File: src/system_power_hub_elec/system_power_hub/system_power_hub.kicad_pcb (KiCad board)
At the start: 6 copper layers, 65 x 65 mm, 127 parts, among them J1 XT90M, J101 SM02B-PASS, J2 XT60F, J3 SM02B-PASS, J4 XT60F, J6 IDC6, J8 XT60F, J9 XT60F, Q1 SSM3K333R, Q10 IRFH7440TRPBF, Q2 Q_Dual_NPN_NPN_E1B1C2E2B2C1, Q3 IRFH7440TRPBF, Q4 IRFH7440TRPBF, Q8 Q_Dual_NPN_NPN_E1B1C2E2B2C1, Q9 IRFH7440TRPBF, U102 TCAN1462V, U2 STM32G474RBT6, U220 MP2459GJ-Z-MS, U230 AP62200TWU, U4 24LC128, Y1 24MHz

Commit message: Draft SPM PCB layout
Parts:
- removed U2: STM32G474RBT6, Package_QFP:LQFP-64_10x10mm_P0.5mm
- added C32: 100n, Capacitor_SMD:C_0603_1608Metric, B.Cu at (141.4, 57.8)
- added C33: 1u, Capacitor_SMD:C_1206_3216Metric, B.Cu at (146.3, 60.5)
- added C34: 100n, Capacitor_SMD:C_0603_1608Metric, B.Cu at (78.1, 128.5)
- added C35: 100n, Capacitor_SMD:C_0603_1608Metric, B.Cu at (73.1, 128.5)
- added C38: 1n, Capacitor_SMD:C_0402_1005Metric, B.Cu at (83.8, 114.4)
- added C39: 1n, Capacitor_SMD:C_0402_1005Metric, B.Cu at (84.1, 124.9)
- added C40: 1n, Capacitor_SMD:C_0402_1005Metric, B.Cu at (66.6, 114.4)
- added C41: 1n, Capacitor_SMD:C_0402_1005Metric, B.Cu at (65.9, 125.0)
- added C42: 100n, Capacitor_SMD:C_0603_1608Metric, B.Cu at (112.4, 128.4)
- added C43: 100n, Capacitor_SMD:C_0603_1608Metric, B.Cu at (107.4, 128.5)
- added C44: 1n, Capacitor_SMD:C_0402_1005Metric, B.Cu at (118.1, 114.3)
- added C45: 1n, Capacitor_SMD:C_0402_1005Metric, B.Cu at (118.3, 124.8)
- added C46: 1n, Capacitor_SMD:C_0402_1005Metric, B.Cu at (100.9, 114.3)
- added C47: 1n, Capacitor_SMD:C_0402_1005Metric, B.Cu at (100.2, 124.9)
- added C48: 1n, Capacitor_SMD:C_0402_1005Metric, B.Cu at (118.3, 128.9)
- added C49: 1n, Capacitor_SMD:C_0402_1005Metric, B.Cu at (100.2, 128.6)
- added C50: 1n, Capacitor_SMD:C_0402_1005Metric, B.Cu at (84.0, 128.9)
- added C51: 1n, Capacitor_SMD:C_0402_1005Metric, B.Cu at (65.9, 128.6)
- added D4: SBR0560S1-7, Diode_SMD:D_SOD-123, B.Cu at (146.2, 53.8)
- added D5: SBR0560S1-7, Diode_SMD:D_SOD-123, B.Cu at (146.2, 57.1)
- added J5: XT30F, Connector_AMASS:AMASS_XT30PW-F_1x02_P2.50mm_Horizontal, F.Cu at (69.3, 117.3)
- added J7: XT30F, Connector_AMASS:AMASS_XT30PW-F_1x02_P2.50mm_Horizontal, F.Cu at (120.8, 117.3)
- added J8: XT30F, Connector_AMASS:AMASS_XT30PW-F_1x02_P2.50mm_Horizontal, F.Cu at (103.6, 117.3)
- added Q10: IRFH7440TRPBF, Bluesat:PQFN_5x6mm_E_SGD, B.Cu at (103.6, 127.6)
- added Q11: IRFH7440TRPBF, Bluesat:PQFN_5x6mm_E_SGD, B.Cu at (69.4, 127.6)
- added Q5: SSM3K333R, Package_TO_SOT_SMD:SOT-23-3, B.Cu at (140.8, 54.3)
- added Q6: Q_Dual_NPN_NPN_E1B1C2E2B2C1, Package_TO_SOT_SMD:SOT-363_SC-70-6, B.Cu at (75.6, 126.9)
- added Q7: IRFH7440TRPBF, Bluesat:PQFN_5x6mm_E_SGD, B.Cu at (87.5, 127.8)
- added Q8: Q_Dual_NPN_NPN_E1B1C2E2B2C1, Package_TO_SOT_SMD:SOT-363_SC-70-6, B.Cu at (109.9, 126.8)
- added Q9: IRFH7440TRPBF, Bluesat:PQFN_5x6mm_E_SGD, B.Cu at (121.7, 127.7)
- added R16: 10k, Resistor_SMD:R_0402_1005Metric, B.Cu at (109.9, 130.0)
- added R18: 100R, Resistor_SMD:R_0402_1005Metric, B.Cu at (141.9, 60.1)
- added R20: 470k, Resistor_SMD:R_0402_1005Metric, B.Cu at (141.9, 62.1)
- added R21: 10k, Resistor_SMD:R_0402_1005Metric, B.Cu at (109.9, 123.6)
- added R22: 470k, Resistor_SMD:R_0402_1005Metric, B.Cu at (112.3, 125.3)
- added R23: 470k, Resistor_SMD:R_0402_1005Metric, B.Cu at (107.5, 125.3)
- added R24: 10k, Resistor_SMD:R_0402_1005Metric, B.Cu at (75.6, 130.1)
- added R25: 10k, Resistor_SMD:R_0402_1005Metric, B.Cu at (75.6, 123.7)
- added R26: 1m, Resistor_SMD:R_2512_6332Metric, B.Cu at (115.6, 127.3)
- added R27: 1m, Resistor_SMD:R_2512_6332Metric, B.Cu at (97.4, 127.5)
- added R28: 470k, Resistor_SMD:R_0402_1005Metric, B.Cu at (78.0, 125.4)
- added R29: 470k, Resistor_SMD:R_0402_1005Metric, B.Cu at (73.2, 125.4)
- added R30: 1m, Resistor_SMD:R_2512_6332Metric, B.Cu at (81.3, 127.4)
- added R31: 1m, Resistor_SMD:R_2512_6332Metric, B.Cu at (63.1, 127.6)
- added U1: STM32G474RBT6, Package_QFP:LQFP-64_10x10mm_P0.5mm, B.Cu at (146.0, 88.9)
- J1: value XT90M -> XT60M; footprint Connector_AMASS:AMASS_XT90PW-M_1x02_P10.90mm_Horizontal -> Connector_AMASS:AMASS_XT60IPW-M_1x03_P7.20mm_Horizontal
- J10: renamed from J9; value XT60F -> XT30F; footprint Connector_AMASS:AMASS_XT60PW-F_1x02_P7.20mm_Horizontal -> Connector_AMASS:AMASS_XT30PW-F_1x02_P2.50mm_Horizontal
- J2, J4: value XT60F -> XT30F; footprint Connector_AMASS:AMASS_XT60PW-F_1x02_P7.20mm_Horizontal -> Connector_AMASS:AMASS_XT30PW-F_1x02_P2.50mm_Horizontal
- J3: value SM02B-PASS -> XT30F; footprint Bluesat:SM02B-PASS -> Connector_AMASS:AMASS_XT30PW-F_1x02_P2.50mm_Horizontal
- J9: renamed from J8; value XT60F -> XT30F; footprint Connector_AMASS:AMASS_XT60PW-F_1x02_P7.20mm_Horizontal -> Connector_AMASS:AMASS_XT30PW-F_1x02_P2.50mm_Horizontal
- moved G*** 103.4 mm to (254.4, 108.5)
- moved C260 96.7 mm to (68.5, 108.8), turned to 180 degrees
- moved C261 91.7 mm to (68.8, 79.4), turned to 180 degrees
- moved J3 88.5 mm to (86.6, 117.3), turned to 180 degrees
- moved J101 78.9 mm to (209.2, 71.3), turned to -90 degrees
- moved R230 76.4 mm to (78.2, 77.4), turned to 0 degrees
- moved R231 75.0 mm to (78.2, 79.0), turned to 180 degrees
- moved R232 73.7 mm to (78.2, 80.6), turned to 180 degrees
- moved C231 72.5 mm to (82.4, 76.8), turned to 0 degrees
- moved C232 71.2 mm to (78.8, 82.8), turned to -90 degrees
- moved U230 69.9 mm to (82.4, 79.6), turned to 180 degrees
- moved C230 66.8 mm to (82.4, 83.2), turned to 0 degrees
- moved L230 66.5 mm to (87.2, 77.8), turned to 90 degrees
- moved D101 65.6 mm to (199.6, 71.3), turned to 180 degrees
- moved C12 64.6 mm to (70.0, 96.9)
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- renumbered C to C1, C to C250, C42 to C52, C43 to C53, C44 to C54, C45 to C55, C46 to C56, C47 to C57, C48 to C58, C49 to C59, Q4 to Q12, Q8 to Q13, Q9 to Q15, Q10 to Q16, Q3 to Q4, R16 to R32, R21 to R33, R22 to R34, R23 to R35, R26 to R36, R27 to R37, U to U240
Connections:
- C15 pad 1: GND -> Net-(U1A-PA2-opamp_vout_0)
- C16 pad 1: GND -> Net-(U1A-PA8-opamp_vout_1)
- C17 pad 1: GND -> Net-(U1A-PA6-opamp_vout_2)
- C18 pad 1: GND -> Net-(U1A-PB11-opamp_vout_3)
- D12 pad 1: Net-(D12-K) -> Vdrive
- J1 pad 1: VBUS -> GND
- J1 pad 2: GND -> VBUS
- J3 pad 1: Vdrive -> /Analog Stuff/vsense_p4
- J3 pad 2: Net-(D12-K) -> Net-(J3-Pin_2)
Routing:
- net /Analog Stuff/vsense_p3: track 87.1 -> 10.5 mm, vias 1 -> 0
- net Vdrive: track 138.0 -> 78.8 mm, vias 12 -> 9
- net /Analog Stuff/vsense_p0: track 68.7 -> 10.4 mm, vias 6 -> 0
- net /Analog Stuff/~{chan0}: track 57.8 -> 0.00 mm, vias 2 -> 1
- net /Analog Stuff/~{chan1}: track 54.5 -> 0.00 mm, vias 2 -> 1
- net /Analog Stuff/vsense_p1: track 54.7 -> 10.5 mm, vias 4 -> 0
- net /Analog Stuff/~{chan2}: track 39.1 -> 0.00 mm, vias 2 -> 1
- net /CANH: track 35.9 -> 0.11 mm
- net /CANL: track 35.4 -> 0.42 mm
- net /dbg.swdio: track 38.9 -> 6.46 mm, vias 2 -> 1
- net /dbg.swclk: track 36.5 -> 5.13 mm, vias 2 -> 1
- net /Analog Stuff/~{chan3}: track 28.4 -> 0.00 mm, vias 2 -> 1
- net /Analog Stuff/clk_in: track 27.5 -> 0.92 mm
- net Net-(U102-TXD): track 24.1 -> 0.07 mm
- net /dbg.swo: track 27.1 -> 3.26 mm, vias 3 -> 1
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- added copper zone on B.Cu, net /Analog Stuff/vsense_p4
- added copper zone on B.Cu, net /Analog Stuff/vsense_p5
- added copper zone on B.Cu, net /Analog Stuff/vsense_p6
- added copper zone on B.Cu, net /Analog Stuff/vsense_p7
- added copper zone on B.Cu, net Net-(J3-Pin_2)
- added copper zone on B.Cu, net Net-(J7-Pin_2)
- added copper zone on B.Cu, net Net-(J8-Pin_2)
- removed copper zone on B.Cu, net Net-(D12-K)
- removed copper zone on B.Cu, net Net-(J2-Pin_2)
- removed copper zone on In3.Cu, net VDD
- removed copper zone on B.Cu, net Vdrive
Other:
- board size 65 x 65 mm -> 66.5 x 77.6 mm
- board text added: "2nd charge pump (?)"
- board text added: "5V + RGB"
- board text added: "CAN"
- board text added: "EEPROM"
- board text added: "SWD"
- board text added: "WIP: Need to fix/swap pinout for xt30 connectors"
- board text added: "WIP: fix pin dir"
- board text added: "WIP: rearrange power circuits"
- board text added: "for opamps"

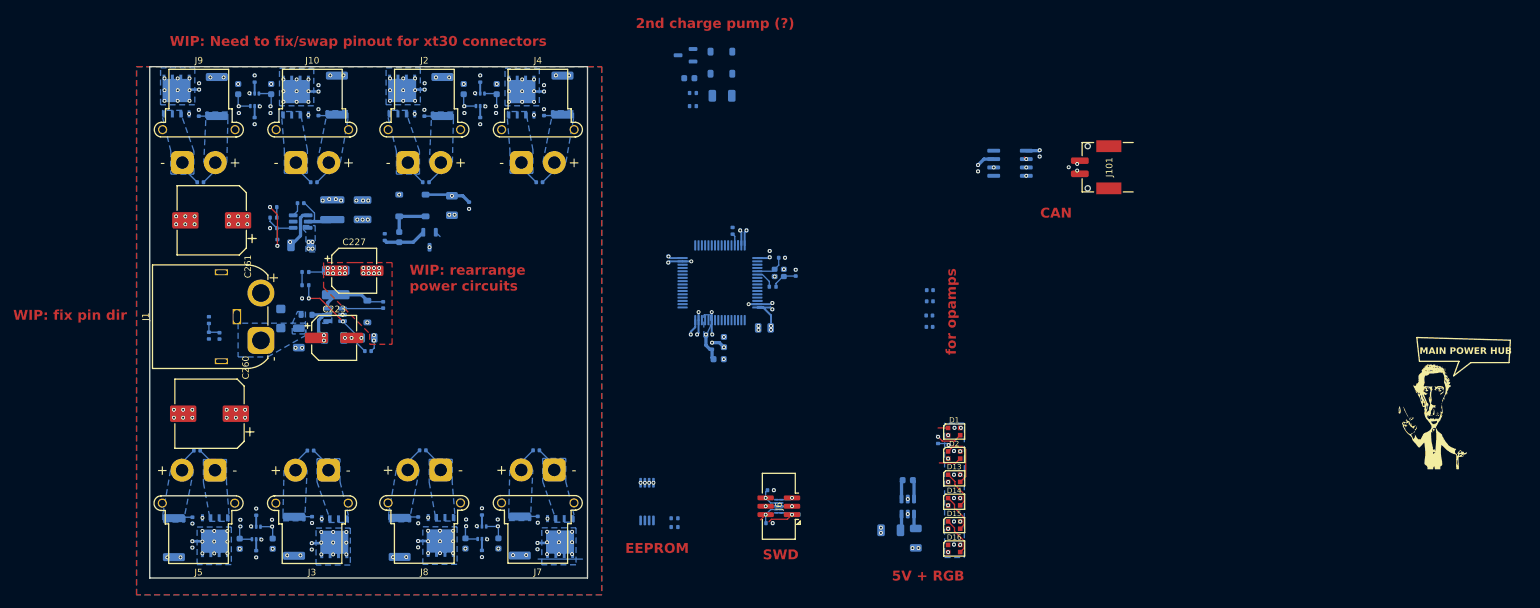
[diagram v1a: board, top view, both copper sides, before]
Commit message: Fixed XT connector routing, rewired power stuff (attempted to), made board smaller, more routing/layout progress
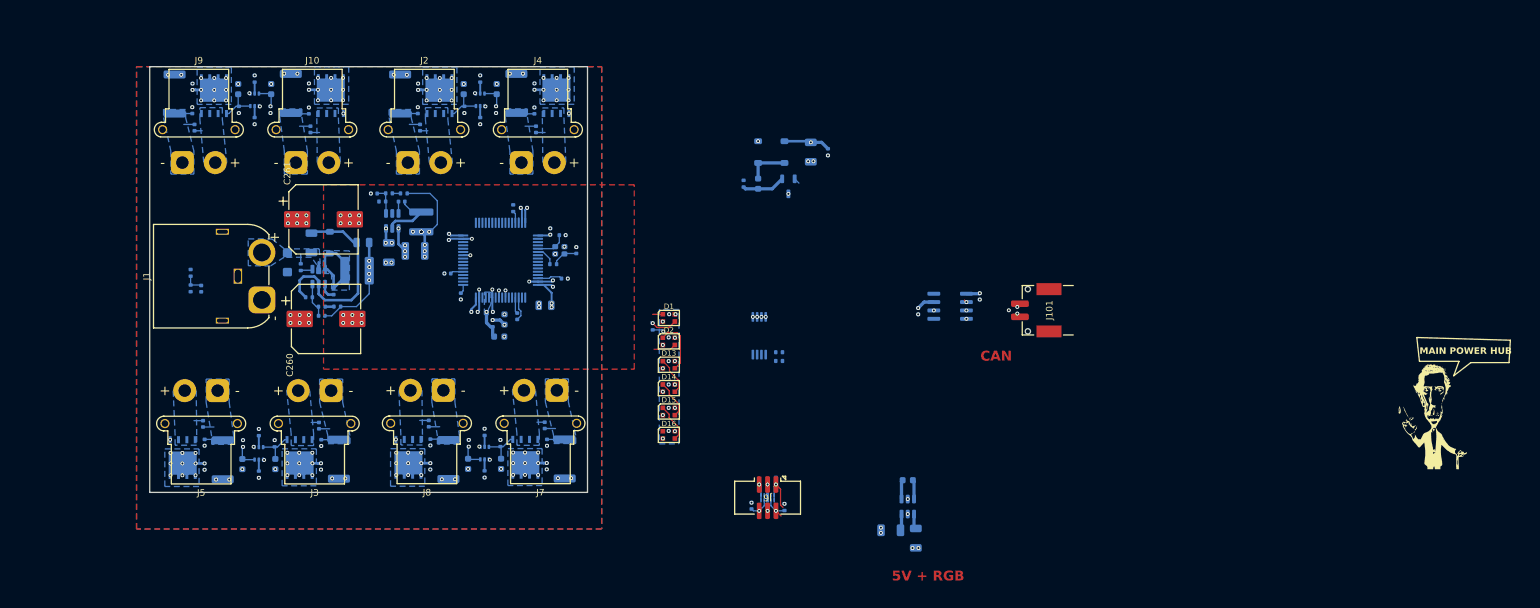
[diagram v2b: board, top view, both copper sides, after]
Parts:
- removed C222, C33: 1u, Capacitor_SMD:C_1206_3216Metric
- removed C223, C227: 68u, Capacitor_SMD:CP_Elec_6.3x7.7
- removed C32: 100n, Capacitor_SMD:C_0603_1608Metric
- removed D4, D5: SBR0560S1-7, Diode_SMD:D_SOD-123
- removed L220: 120R, Resistor_SMD:R_0603_1608Metric
- removed Q5: SSM3K333R, Package_TO_SOT_SMD:SOT-23-3
- removed R20: 470k, Resistor_SMD:R_0402_1005Metric
- R18: value 100R -> 100k
- moved C16 73.4 mm to (104.7, 87.5), turned to 0 degrees
- moved C18 71.2 mm to (106.7, 90.9), turned to -90 degrees
- moved R18 65.1 mm to (82.4, 86.5), turned to -90 degrees
- moved C17 62.6 mm to (115.2, 94.0), turned to -90 degrees
- moved C15 55.5 mm to (122.4, 88.2), turned to 0 degrees
- moved C36 55.1 mm to (151.8, 73.8)
- moved C37 55.1 mm to (159.8, 69.0)
- moved D11 55.1 mm to (151.8, 69.0)
- moved D12 55.1 mm to (155.8, 69.0)
- moved Q1 55.1 mm to (156.4, 74.2)
- moved R19 55.1 mm to (162.4, 69.0)
- moved R8 55.1 mm to (149.6, 73.8)
- moved C2 46.6 mm to (138.7, 97.2)
- moved C26 46.6 mm to (138.8, 93.7)
- moved C27 46.6 mm to (138.7, 100.8)
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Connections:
- R18 pad 1: +12V -> VBUS
- R18 pad 2: Net-(Q5-D) -> Net-(U220-EN)
- U220 pad 4: /Power/VBUS_{FLT} -> Net-(U220-EN)
- U220 pad 5: /Power/VBUS_{FLT} -> VBUS
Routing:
- net GND: track 25.0 -> 53.1 mm, vias 131 -> 116
- net VBUS: track 42.1 -> 21.7 mm
- net +12V: track 6.39 -> 18.6 mm, vias 14 -> 7
- net Net-(U1A-PC5-opamp_vinm_0): track 0.00 -> 11.8 mm, vias 0 -> 2
- net /Power/12V_{FB}: track 14.6 -> 5.38 mm, vias 2 -> 0
- net VDD: track 28.6 -> 36.9 mm, vias 22 -> 26
- net Net-(U1A-PB1-opamp_vinm_3): track 0.00 -> 7.44 mm, vias 0 -> 2
- net /Power/VBUS_{FLT}: track 7.13 -> 0.00 mm, vias 2 -> 0
- net Net-(U1A-PA8-opamp_vout_1): track 0.00 -> 6.95 mm, vias 0 -> 2
- net Net-(Q8A-C1): track 12.7 -> 5.98 mm, vias 2 -> 0
- net Net-(Q13A-C1): track 12.7 -> 5.98 mm, vias 2 -> 0
- net Net-(Q2A-C1): track 12.7 -> 5.98 mm, vias 2 -> 0
- net Net-(Q6A-C1): track 12.7 -> 5.98 mm, vias 2 -> 0
- net /Analog Stuff/vsense_p4: track 10.4 -> 4.32 mm
- net /Analog Stuff/vsense_p2: track 10.4 -> 4.32 mm
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- added copper zone on B.Cu, net /Power/12V_{SW}
- added copper zone on B.Cu, net Net-(J2-Pin_2)
- added copper zone on B.Cu, net Net-(J5-Pin_2)
- added copper zone on In3.Cu, net VDD
- removed copper zone on B.Cu, net +12V
- removed copper zone on F.Cu, net +12V
- removed copper zone on B.Cu, net /Power/VBUS_{FLT}
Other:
- board size 66.5 x 77.6 mm -> 66.5 x 64.6 mm
- board text removed: "2nd charge pump (?)"
- board text removed: "EEPROM"
- board text removed: "SWD"
- board text removed: "WIP: Need to fix/swap pinout for xt30 connectors"
- board text removed: "WIP: fix pin dir"
- board text removed: "WIP: rearrange power circuits"
- board text removed: "for opamps"

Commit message: Draft layout done, need to continue routing and decide on GPIO
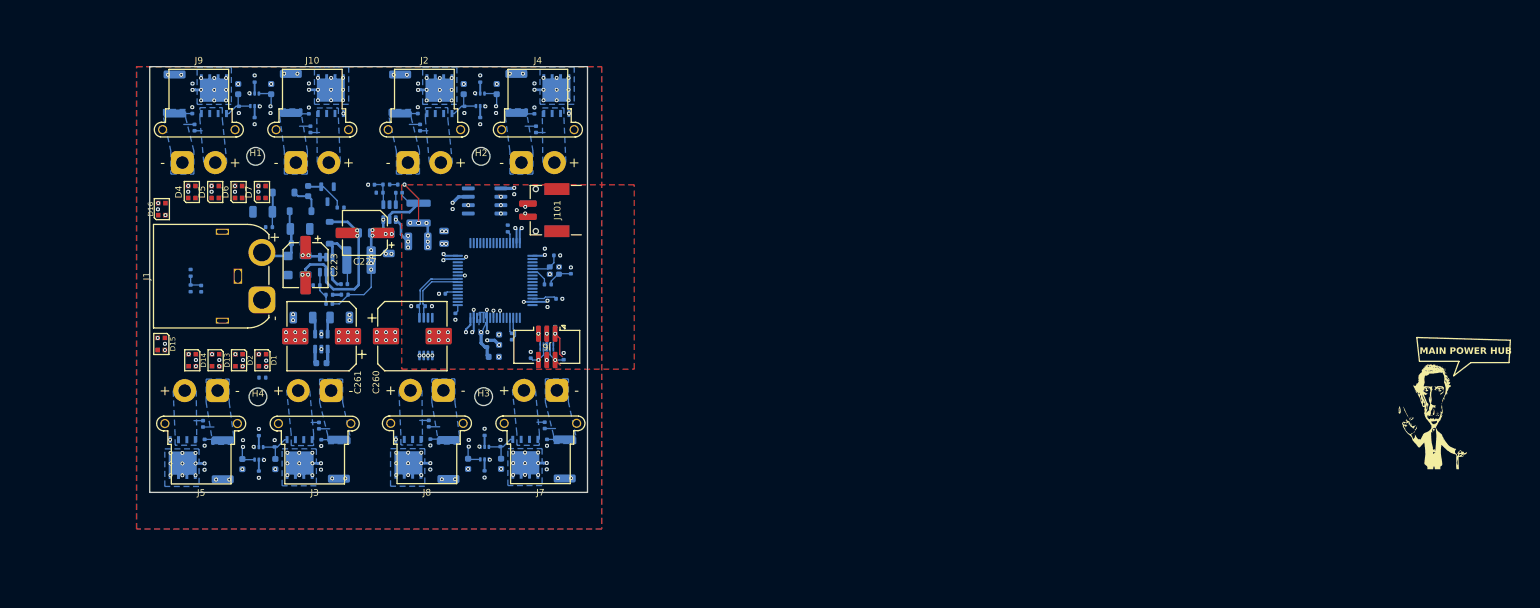
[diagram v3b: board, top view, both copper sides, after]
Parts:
- removed R18: 100k, Resistor_SMD:R_0402_1005Metric
- added C222: 1u, Capacitor_SMD:C_1206_3216Metric, B.Cu at (83.1, 86.2)
- added C223: 68u, Capacitor_SMD:CP_Elec_6.3x7.7, F.Cu at (83.1, 86.2)
- added C227: 68u, Capacitor_SMD:CP_Elec_6.3x7.7, F.Cu at (92.1, 81.3)
- added C32: 220n, Capacitor_SMD:C_0402_1005Metric, B.Cu at (65.3, 74.6)
- added C33: 220n, Capacitor_SMD:C_0402_1005Metric, B.Cu at (68.8, 74.6)
- added C60: 220n, Capacitor_SMD:C_0402_1005Metric, B.Cu at (72.4, 74.6)
- added C61: 220n, Capacitor_SMD:C_0402_1005Metric, B.Cu at (75.9, 74.6)
- added D4: WS2812B-2020, LED_SMD:LED_WS2812B-2020_PLCC4_2.0x2.0mm, F.Cu at (65.8, 75.1)
- added D5: WS2812B-2020, LED_SMD:LED_WS2812B-2020_PLCC4_2.0x2.0mm, F.Cu at (69.4, 75.1)
- added D6: WS2812B-2020, LED_SMD:LED_WS2812B-2020_PLCC4_2.0x2.0mm, F.Cu at (72.9, 75.1)
- added D7: WS2812B-2020, LED_SMD:LED_WS2812B-2020_PLCC4_2.0x2.0mm, F.Cu at (76.5, 75.1)
- added H1: MountingHole, Bluesat:M2.5, F.Cu at (75.5, 69.7)
- added H2: MountingHole, Bluesat:M2.5, F.Cu at (109.8, 69.7)
- added H3: MountingHole, Bluesat:M2.5, F.Cu at (110.1, 106.2)
- added H4: MountingHole, Bluesat:M2.5, F.Cu at (75.9, 106.2)
- added L220: 120R, Resistor_SMD:R_0603_1608Metric, B.Cu at (81.8, 82.9)
- moved C242 98.9 mm to (82.7, 94.2), turned to 0 degrees
- moved U240 92.5 mm to (85.5, 97.8), turned to -90 degrees
- moved C241 90.8 mm to (85.5, 101.1), turned to 180 degrees
- moved C240 89.7 mm to (88.3, 94.2), turned to 180 degrees
- moved R19 85.6 mm to (77.5, 80.4), turned to 180 degrees
- moved C30 85.2 mm to (60.7, 77.2), turned to 90 degrees
- moved D16 84.3 mm to (61.3, 77.7), turned to 90 degrees
- moved C37 83.7 mm to (76.6, 78.1), turned to 0 degrees
- moved D15 77.7 mm to (61.2, 98.2), turned to -90 degrees
- moved C29 77.5 mm to (61.8, 98.6), turned to -90 degrees
- moved D12 76.3 mm to (79.8, 75.2), turned to 0 degrees
- moved J101 76.2 mm to (125.5, 77.8)
- moved D101 76.2 mm to (115.8, 77.8)
- moved D14 72.5 mm to (65.9, 100.6), turned to -90 degrees
- moved C25 72.5 mm to (105.4, 77.2)
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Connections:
- D16 pad 1: unconnected-(D16-DOUT-Pad1) -> Net-(D16-DOUT)
- U220 pad 4: Net-(U220-EN) -> /Power/VBUS_{FLT}
- U220 pad 5: VBUS -> /Power/VBUS_{FLT}
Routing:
- net GND: track 53.1 -> 65.5 mm, vias 116 -> 120
- net Net-(U1A-PC9-i2c_sda): track 0.00 -> 10.9 mm
- net Net-(U1A-PC5-opamp_vinm_0): track 11.8 -> 1.09 mm
- net Net-(U1A-PC8-i2c_sclk): track 0.00 -> 10.2 mm
- net VDD: track 36.9 -> 27.9 mm, vias 26 -> 29
- net VBUS: track 21.7 -> 30.5 mm, vias 93 -> 92
- net Net-(D13-DIN): track 8.43 -> 0.00 mm
- net Net-(U1A-PB1-opamp_vinm_3): track 7.44 -> 1.09 mm
- net Net-(D14-DOUT): track 5.90 -> 0.00 mm
- net Net-(D13-DOUT): track 5.90 -> 0.00 mm
- net Net-(D15-DOUT): track 5.90 -> 0.00 mm
- net /Power/VBUS_{FLT}: track 0.00 -> 5.30 mm, vias 0 -> 2
- net Net-(D1-DOUT): track 4.97 -> 0.00 mm
- net Net-(D1-DIN): track 4.35 -> 0.00 mm, vias 1 -> 0
- net /Power/12V_{SW}: track 14.1 -> 10.2 mm
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- removed copper zone on B.Cu, net +5V
- removed copper zone on B.Cu, net /Power/12V_{SW}
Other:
- board text removed: "5V + RGB"
- board text removed: "CAN"

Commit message: Routed everything except GPIO
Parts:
- moved R17 37.2 mm to (104.2, 78.3), turned to -90 degrees
- moved C7 4.37 mm to (101.4, 85.4), turned to 0 degrees
- moved C26 1.95 mm to (75.5, 100.1), turned to 90 degrees
- moved C2 1.92 mm to (71.9, 100.2), turned to 90 degrees
- moved C18 1.89 mm to (104.2, 93.0)
- moved C28 1.84 mm to (64.8, 100.2), turned to 90 degrees
- moved C27 1.84 mm to (68.4, 100.2), turned to 90 degrees
- moved C33 1.35 mm to (69.7, 75.6), turned to -90 degrees
- moved C60 1.35 mm to (73.2, 75.6), turned to -90 degrees
- moved C32 1.35 mm to (66.1, 75.6), turned to -90 degrees
- moved C61 1.35 mm to (76.8, 75.6), turned to -90 degrees
- moved C30 1.07 mm to (61.7, 77.1), turned to 0 degrees
- moved C29 1.00 mm to (61.7, 97.6), turned to 0 degrees
- moved D1 0.50 mm to (76.0, 100.6), turned to 90 degrees
- moved D13 0.50 mm to (69.0, 100.6), turned to 90 degrees
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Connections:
- U102 pad 8: VDD -> GND
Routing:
- net Vdrive: track 77.0 -> 251.6 mm, vias 8 -> 12
- net +5V: track 5.41 -> 95.2 mm, vias 11 -> 14
- net Net-(D1-DIN): track 0.00 -> 57.4 mm, vias 0 -> 2
- net VDD: track 27.9 -> 65.4 mm, vias 29 -> 30
- net /dbg.nrst: track 3.98 -> 28.2 mm, vias 1 -> 2
- net /dbg.swclk: track 5.13 -> 29.3 mm, vias 1 -> 2
- net Net-(D15-DOUT): track 0.00 -> 20.2 mm
- net /dbg.swdio: track 6.46 -> 25.7 mm, vias 1 -> 2
- net GND: track 65.5 -> 48.5 mm, vias 120 -> 121
- net /dbg.swo: track 3.26 -> 18.8 mm, vias 1 -> 2
- net Net-(U102-RXD): track 0.00 -> 13.9 mm, vias 0 -> 2
- net Net-(U102-TXD): track 0.07 -> 12.3 mm, vias 0 -> 2
- net Net-(U1A-PC5-opamp_vinm_0): track 1.09 -> 11.7 mm
- net Net-(U1A-PB1-opamp_vinm_3): track 1.09 -> 9.52 mm
- net /CANL: track 0.42 -> 7.86 mm
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- added copper zone on B.Cu, net /Power/VBUS_{FLT}

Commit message: More basic routing updates
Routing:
- net /Analog Stuff/clk_in: track 0.00 -> 17.6 mm, vias 0 -> 2
- net Net-(U102-TXD): track 12.3 -> 14.7 mm, vias 2 -> 0
- net GND: track 48.5 -> 47.0 mm, vias 121 -> 124
- net Net-(D1-DIN): track 57.4 -> 56.3 mm, vias 2 -> 3
- net Net-(U102-RXD): track 13.9 -> 14.9 mm, vias 2 -> 0
